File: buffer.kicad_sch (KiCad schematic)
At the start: 5 parts, among them U6 74LVC1G17

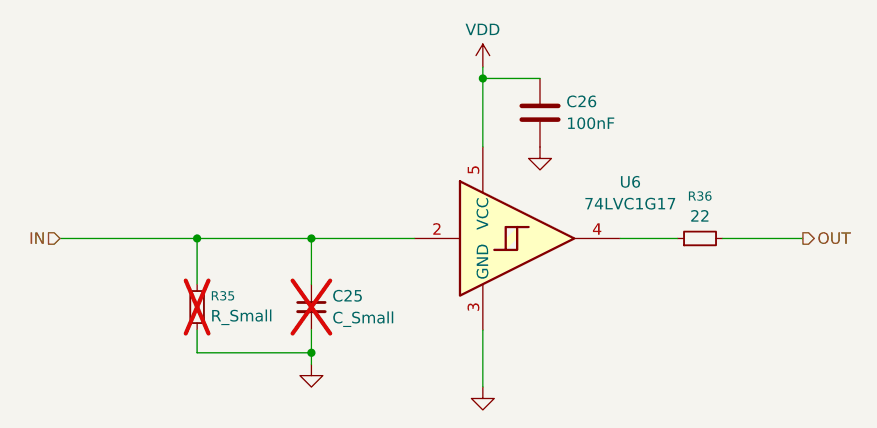
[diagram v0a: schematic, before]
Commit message: adding subproject, breakout board for nucleo
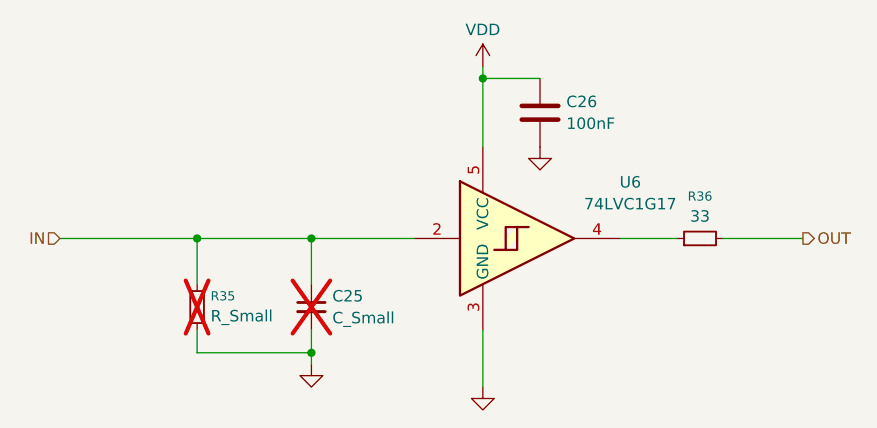
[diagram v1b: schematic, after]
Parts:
- R36: value 22 -> 33
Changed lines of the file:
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@@
 			)
 		)
-		(property "Value" "22"
+		(property "Value" "33"
 			(at 142.24 73.7432 90)
 			(effects
